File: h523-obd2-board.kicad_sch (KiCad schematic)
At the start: 68 parts, among them J1 Conn_02x05_Odd_Even, J2 Conn_01x03, J3 Conn_01x03, J4 Conn_01x03, J5 Conn_01x03, J6 Conn_01x03, J7 Conn_01x03, J8 Conn_01x03, J9 Conn_01x03, Q1 AO3400A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

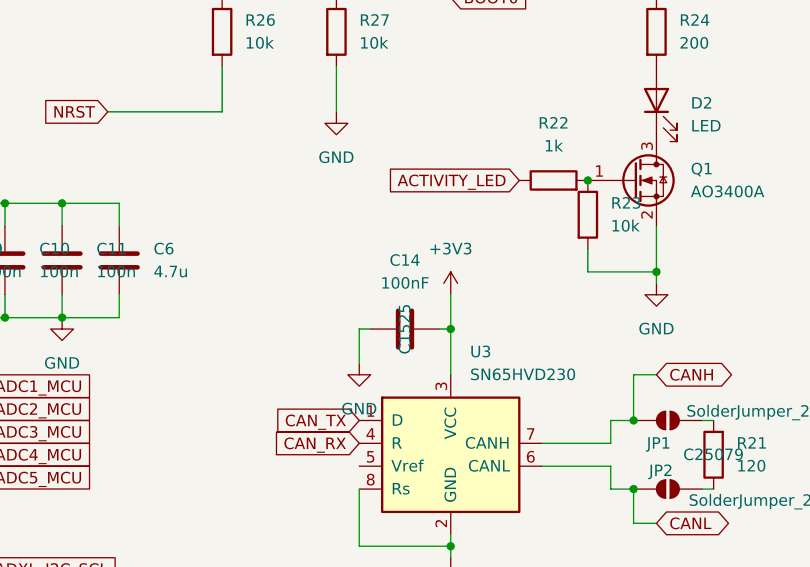
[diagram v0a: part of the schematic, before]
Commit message: updated BOM for supporting parts
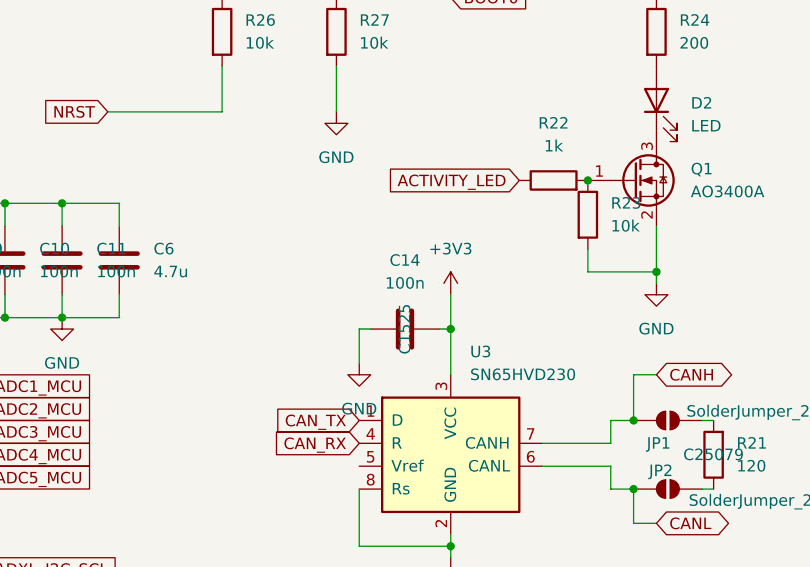
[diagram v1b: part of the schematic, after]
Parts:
- C14: value 100nF -> 100n
- C17: LCSC C19666 -> C15849
- R28, R29: LCSC C25744 -> C25900

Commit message: PROTO A manufactured
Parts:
- removed U5: ADXL345, JLCLibrary:ADXL345, symbol JLCLibrary:ADXL345BCCZ-RL
- added C18, C19: 6.8n, Capacitor_SMD:C_0402_1005Metric, symbol Device:C
- added J10: Conn_01x08, Connector_PinHeader_2.54mm:PinHeader_1x08_P2.54mm_Vertical, symbol Connector_Generic:Conn_01x08
- added R36, R37: 4.7k, Resistor_SMD:R_0402_1005Metric, symbol Device:R
- C12, C13: LCSC C12530 -> C23630
- C15, C16: value 100n -> 6.8n; LCSC C1525 -> C1542
- C17: value 1u -> 6.8n; footprint Capacitor_SMD:C_0603_1608Metric -> Capacitor_SMD:C_0402_1005Metric; LCSC C15849 -> C1542
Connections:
- net +3V3: now also J10.2 (Pin_2), R36.1, R37.1; no longer C15.1, C16.1, C17.1
- net ADC1_MCU: now also C15.2
- net ADC2_MCU: now also C16.2
- net ADC3_MCU: now also C17.2
- net ADC4_MCU: now also C18.2
- net ADC5_MCU: now also C19.2
- net ADXL_I2C_SCL: now also J10.8 (Pin_8)
- net ADXL_I2C_SDA: now also J10.7 (Pin_7)
- net GND: now also C15.1, C16.1, C17.1, C18.1, C19.1, J10.1 (Pin_1); no longer C15.2, C16.2, C17.2
- net LCD_I2C_SCL: now also R37.2
- net LCD_I2C_SDA: now also R36.2
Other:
- moved on the sheet: C14, JP1, JP2, R21, R28, R29, U3
